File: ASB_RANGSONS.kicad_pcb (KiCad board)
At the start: 2 copper layers, 28 parts, among them P1 MMD_FRC_34PIN, P10 SSD_FRC_20PIN, P2 CONN _1_20, P3 CONN_21_40, P4 CONN_41_60, P5 CONN_61_80, P6 MMD_ROW, P7 PWR_5V, P8 ETH_CON, P9 PWR_12V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

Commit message: MMD_CONTROL_IS_MODIFIED
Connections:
- P1 pad 33: /34 -> (no net)
- P1 pad 34: (no net) -> /34
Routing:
- net /34: track 54.5 -> 55.8 mm
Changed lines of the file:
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@@
     (links 130)
     (no_connects 0)
-    (area 107.8816 67.311599 274.820167 167.7)
+    (area 109.852217 67.311599 274.820167 167.7)
     (thickness 1.6)
     (drawings 20)
@@
   (net 69 N-0000016)
   (net 70 N-000004)
-  (net 71 N-0000077)
-  (net 72 N-0000078)
-  (net 73 N-0000079)
-  (net 74 N-0000080)
-  (net 75 N-0000081)
-  (net 76 N-0000082)
-  (net 77 N-0000083)
-  (net 78 N-0000084)
+  (net 71 N-0000076)
+  (net 72 N-0000077)
+  (net 73 N-0000078)
+  (net 74 N-0000079)
+  (net 75 N-0000080)
+  (net 76 N-0000081)
+  (net 77 N-0000082)
+  (net 78 N-0000083)
   (net_class Default "This is the default net class."
     (clearance 0.17)
@@
     (add_net N-0000016)
     (add_net N-000004)
+    (add_net N-0000076)
     (add_net N-0000077)
     (add_net N-0000078)
@@
     (add_net N-0000082)
     (add_net N-0000083)
-    (add_net N-0000084)
   )
   (net_class Decoder ""
@@
     (pad 1 thru_hole rect (at -8.89 0) (size 1.8 1.8) (drill 0.8128)
       (layers *.Cu *.Mask F.SilkS)
-      (net 71 N-0000077)
+      (net 71 N-0000076)
     )
     (pad 2 thru_hole circle (at -6.35 0) (size 1.8 1.8) (drill 0.8128)
       (layers *.Cu *.Mask F.SilkS)
-      (net 72 N-0000078)
+      (net 72 N-0000077)
     )
     (pad 3 thru_hole circle (at -3.81 0) (size 1.8 1.8) (drill 0.8128)
       (layers *.Cu *.Mask F.SilkS)
-      (net 73 N-0000079)
+      (net 73 N-0000078)
     )
     (pad 4 thru_hole circle (at -1.27 0) (size 1.8 1.8) (drill 0.8128)
       (layers *.Cu *.Mask F.SilkS)
-      (net 74 N-0000080)
+      (net 74 N-0000079)
     )
     (pad 5 thru_hole circle (at 1.27 0) (size 1.8 1.8) (drill 0.8128)
       (layers *.Cu *.Mask F.SilkS)
-      (net 75 N-0000081)
+      (net 75 N-0000080)
     )
     (pad 6 thru_hole circle (at 3.81 0) (size 1.8 1.8) (drill 0.8128)
       (layers *.Cu *.Mask F.SilkS)
-      (net 76 N-0000082)
+      (net 76 N-0000081)
     )
     (pad 7 thru_hole circle (at 6.35 0) (size 1.8 1.8) (drill 0.8128)
       (layers *.Cu *.Mask F.SilkS)
-      (net 77 N-0000083)
+      (net 77 N-0000082)
     )
     (pad 8 thru_hole circle (at 8.89 0) (size 1.8 1.8) (drill 0.8128)
       (layers *.Cu *.Mask F.SilkS)
-      (net 78 N-0000084)
+      (net 78 N-0000083)
     )
   )
@@
     (pad 33 thru_hole circle (at 20.32 1.27 90) (size 1.524 1.524) (drill 0.9144)
       (layers *.Cu *.Mask F.SilkS)
+    )
+    (pad 34 thru_hole circle (at 20.32 -1.27 90) (size 1.524 1.524) (drill 0.9144)
+      (layers *.Cu *.Mask F.SilkS)
       (net 12 /34)
-    )
-    (pad 34 thru_hole circle (at 20.32 -1.27 90) (size 1.524 1.524) (drill 0.9144)
-      (layers *.Cu *.Mask F.SilkS)
     )
     (pad "" thru_hole circle (at 29.21 0.254 90) (size 5.461 5.461) (drill 2.6924)
@@
     (pad 11 thru_hole circle (at 7.62 -3.81) (size 1.397 1.397) (drill 0.8128)
       (layers *.Cu *.Mask F.SilkS)
-      (net 78 N-0000084)
+      (net 78 N-0000083)
     )
     (pad 12 thru_hole circle (at 5.08 -3.81) (size 1.397 1.397) (drill 0.8128)
       (layers *.Cu *.Mask F.SilkS)
-      (net 77 N-0000083)
+      (net 77 N-0000082)
     )
     (pad 13 thru_hole circle (at 2.54 -3.81) (size 1.397 1.397) (drill 0.8128)
       (layers *.Cu *.Mask F.SilkS)
-      (net 76 N-0000082)
+      (net 76 N-0000081)
     )
     (pad 14 thru_hole circle (at 0 -3.81) (size 1.397 1.397) (drill 0.8128)
       (layers *.Cu *.Mask F.SilkS)
-      (net 75 N-0000081)
+      (net 75 N-0000080)
     )
     (pad 15 thru_hole circle (at -2.54 -3.81) (size 1.397 1.397) (drill 0.8128)
       (layers *.Cu *.Mask F.SilkS)
-      (net 74 N-0000080)
+      (net 74 N-0000079)
     )
     (pad 16 thru_hole circle (at -5.08 -3.81) (size 1.397 1.397) (drill 0.8128)
       (layers *.Cu *.Mask F.SilkS)
-      (net 73 N-0000079)
+      (net 73 N-0000078)
     )
     (pad 17 thru_hole circle (at -7.62 -3.81) (size 1.397 1.397) (drill 0.8128)
       (layers *.Cu *.Mask F.SilkS)
-      (net 72 N-0000078)
+      (net 72 N-0000077)
     )
     (pad 18 thru_hole circle (at -10.16 -3.81) (size 1.397 1.397) (drill 0.8128)
       (layers *.Cu *.Mask F.SilkS)
-      (net 71 N-0000077)
+      (net 71 N-0000076)
     )
     (model dil/dil_18.wrl
@@
   (segment (start 162.941 123.1646) (end 172.3771 123.1646) (width 0.508) (layer B.Cu) (net 11))
   (segment (start 160.8328 125.2728) (end 162.941 123.1646) (width 0.508) (layer B.Cu) (net 11))
-  (segment (start 185.2168 92.71) (end 185.2168 89.7382) (width 0.508) (layer F.Cu) (net 12))
-  (segment (start 194.945 123.2662) (end 191.9732 126.238) (width 0.508) (layer F.Cu) (net 12))
-  (segment (start 194.945 87.63) (end 194.945 123.2662) (width 0.508) (layer F.Cu) (net 12))
-  (segment (start 193.675 86.36) (end 194.945 87.63) (width 0.508) (layer F.Cu) (net 12))
-  (segment (start 188.595 86.36) (end 193.675 86.36) (width 0.508) (layer F.Cu) (net 12))
-  (segment (start 185.2168 89.7382) (end 188.595 86.36) (width 0.508) (layer F.Cu) (net 12))
+  (segment (start 191.9732 126.238) (end 192.278 126.238) (width 0.508) (layer F.Cu) (net 12))
+  (segment (start 189.5348 85.852) (end 182.6768 92.71) (width 0.508) (layer F.Cu) (net 12))
+  (segment (start 193.548 85.852) (end 189.5348 85.852) (width 0.508) (layer F.Cu) (net 12))
+  (segment (start 194.564 86.868) (end 193.548 85.852) (width 0.508) (layer F.Cu) (net 12))
+  (segment (start 194.564 123.952) (end 194.564 86.868) (width 0.508) (layer F.Cu) (net 12))
+  (segment (start 192.278 126.238) (end 194.564 123.952) (width 0.508) (layer F.Cu) (net 12))
   (segment (start 185.2168 128.27) (end 185.1533 128.27) (width 0.381) (layer F.Cu) (net 13))
   (segment (start 160.8328 120.5611) (end 160.8328 118.364) (width 0.381) (layer F.Cu) (net 13))
@@
     (polygon
       (pts
-        (xy 199.644 156.972) (xy 110.236 156.972) (xy 110.236 67.564) (xy 199.644 67.564)
+        (xy 199.644 68.072) (xy 199.644 156.972) (xy 110.744 156.972) (xy 110.744 68.072)
       )
     )
@@
     (polygon
       (pts
-        (xy 199.644 67.564) (xy 199.644 156.972) (xy 110.236 156.972) (xy 110.236 67.564) (xy 110.744 67.564)
+        (xy 110.744 68.072) (xy 110.744 156.972) (xy 199.644 156.972) (xy 199.644 68.072)
       )
     )

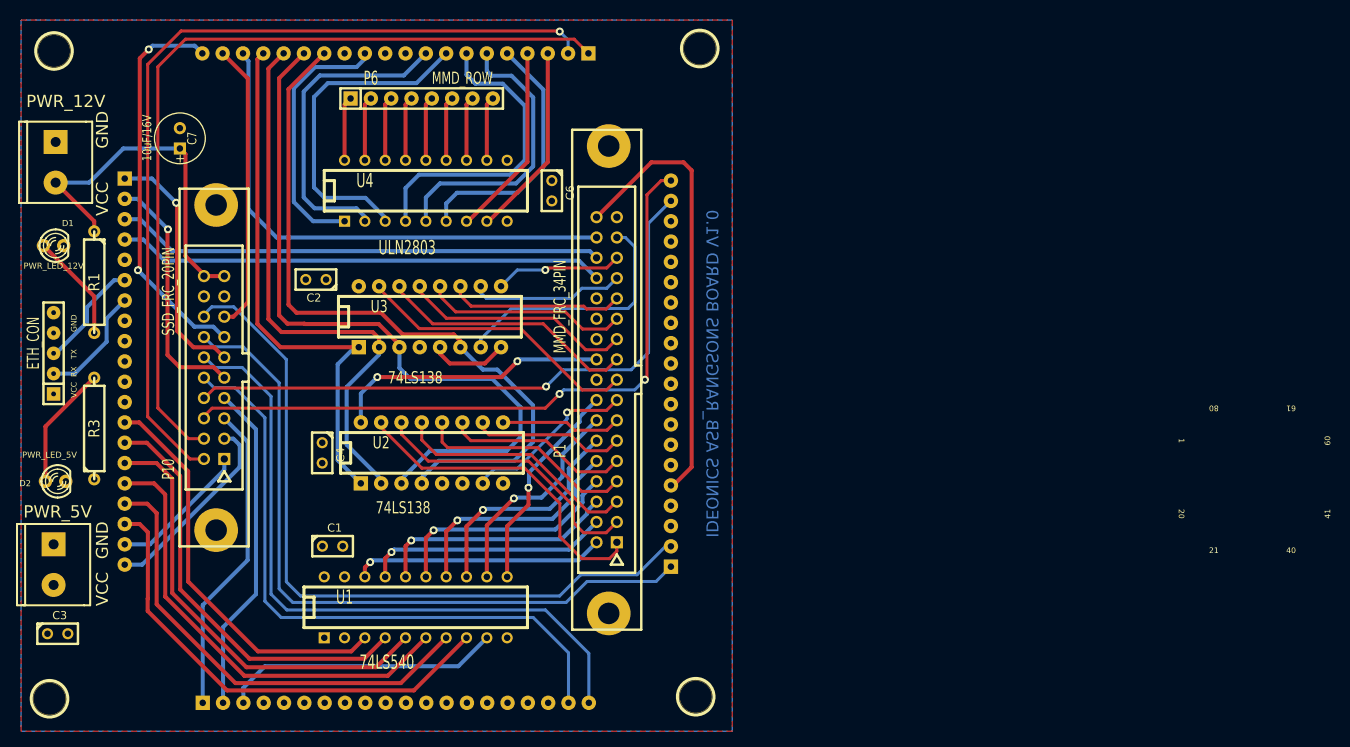
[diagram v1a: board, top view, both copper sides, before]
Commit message: Data lines modified as per led latch schematic
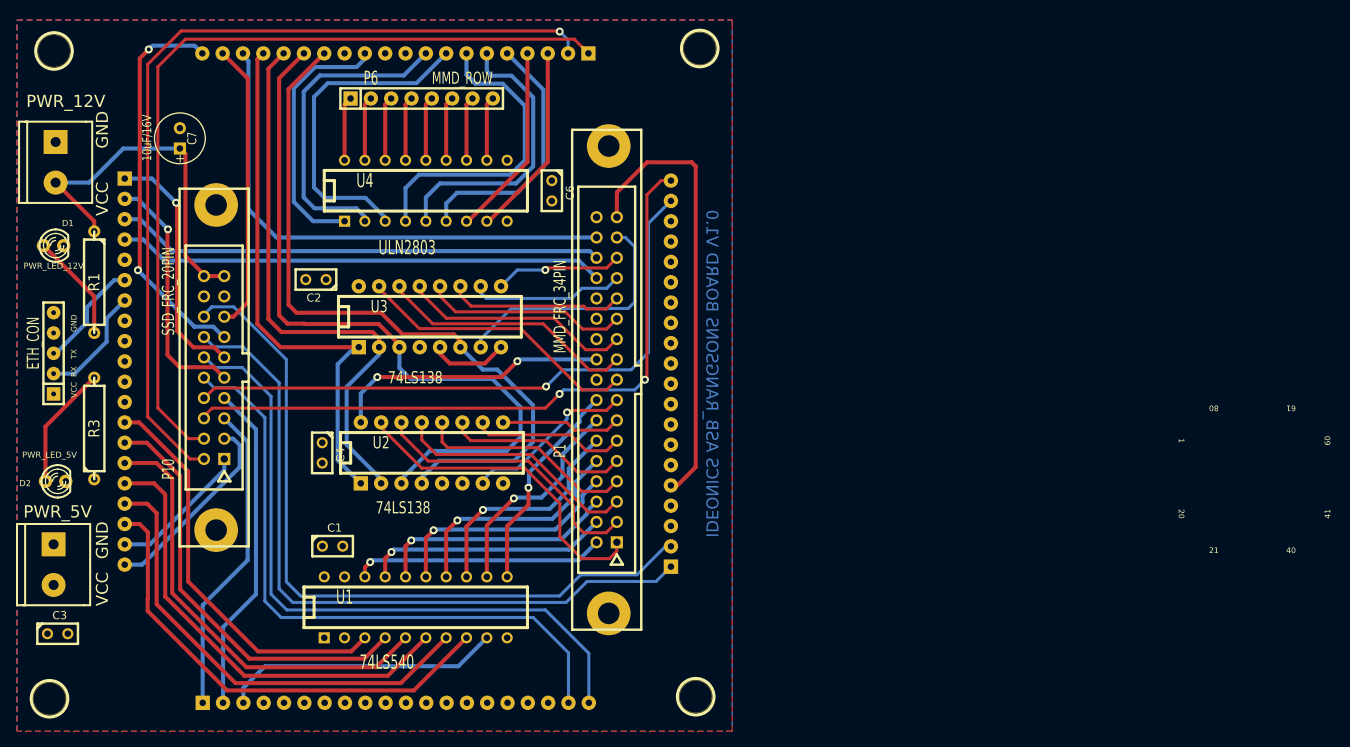
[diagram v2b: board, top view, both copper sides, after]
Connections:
- P1 pad 10: /E -> /D
- P1 pad 12: /F -> /C
- P1 pad 14: /G -> /B
- P1 pad 16: /H -> /A
- P1 pad 2: /A -> /H
- P1 pad 33: (no net) -> /MMD_CONTROL
- P1 pad 34: /34 -> (no net)
- P1 pad 4: /B -> /G
- P1 pad 6: /C -> /F
- P1 pad 8: /D -> /E
- P4 pad 5: /34 -> /MMD_CONTROL
- U1 pad 11: /H -> /A
- U1 pad 12: /G -> /B
- U1 pad 13: /F -> /C
- U1 pad 14: /E -> /D
- U1 pad 15: /D -> /E
- U1 pad 16: /C -> /F
- U1 pad 17: /B -> /G
- U1 pad 18: /A -> /H
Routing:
- net /MMD_CONTROL: track 0.00 -> 56.4 mm
- net /34: track 55.8 -> 0.00 mm
- net /H: track 26.7 -> 31.4 mm
- net /A: track 31.4 -> 26.7 mm
- net /G: track 27.2 -> 30.6 mm
- net /B: track 30.6 -> 27.2 mm
- net /F: track 28.6 -> 30.2 mm
- net /C: track 30.2 -> 28.6 mm
- net /E: track 29.1 -> 29.6 mm
- net /D: track 29.6 -> 29.1 mm
